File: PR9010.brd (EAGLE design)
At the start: 100 x 80 mm, 58 parts, among them J1 AVR_SPI_PRG_6NS, U1 SI4703, U2 Tiny85-20-SMT, Y1 32.768kHz

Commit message: Sch Updates
Continuing to update the PR9010 sch
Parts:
- removed ESD: CM1213A-01S, PubRadioLib:SOT23-3
- added D1: (no value), SparkFun-DiscreteSemi:SOT23
- added U$1, U$2: BK-92_MPD_AA_BATT_CLIP, PR_Libraries:BK-92_MPD_AA_BATT_CLIP
- moved LID 139.4 mm to (64.3, 32.0)
- moved GND 128.5 mm to (53.6, 6.86)
- moved AMP_O 125.3 mm to (36.8, 9.40), turned to 270 degrees
- moved GND33 118.9 mm to (53.6, 10.4)
- moved C18 115.6 mm to (29.0, 4.06), turned to 270 degrees
- moved U$5 113.6 mm to (47.5, 50.3), turned to 270 degrees
- moved C17 108.2 mm to (22.1, 10.9)
- moved GND31 108.1 mm to (53.6, 14.2)
- moved C16 106.3 mm to (22.1, 8.89)
- moved C9 106.1 mm to (32.5, 9.40)
- moved R1 105.6 mm to (65.0, 29.0), turned to 180 degrees
- moved C11 104.7 mm to (26.2, 11.9), turned to 90 degrees
- moved C10 100.7 mm to (24.6, 50.5), turned to 270 degrees
- moved C20 100.5 mm to (65.0, 26.2), turned to 180 degrees
- moved C12 100.3 mm to (22.1, 4.83)
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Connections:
- removed net N$10: C1.1, C13.1, C2.1, C6.1, L3.2
- removed net N$19: ANT.P$1, C10.1, C8.1, ESD.1
- new net N$13: U$1.NEG, U$1.NEG@2, U$2.POS, U$2.POS@2
- new net N$14: ANT.P$1, D1.1
- new net N$15: PWRIN.1, U$1.POS, U$1.POS@2, U$5.SW_OUT
- new net N$17: C10.1, C8.1, D1.2
- net 3.3V: no longer PWRIN.1, U$5.SW_OUT
- net GND: now also D1.3, U$2.NEG, U$2.NEG@2; no longer ESD.2, ESD.3
- net N$9: now also C1.1, C13.1, C2.1, C6.1, L3.2
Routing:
- net SDIO: track 0.00 -> 49.5 mm, vias 0 -> 2
- net SCLK: track 0.00 -> 49.0 mm
- net 3.3V: track 0.00 -> 24.4 mm, vias 0 -> 4
- net N$9: track 0.00 -> 15.6 mm, vias 0 -> 2
- net !RST-L: track 0.00 -> 14.3 mm
- net N$18: track 0.00 -> 14.0 mm
- net SDIO-L: track 0.00 -> 12.7 mm
- net PB1: track 0.00 -> 12.6 mm, vias 0 -> 2
- net !SEN-L: track 0.00 -> 12.2 mm
- net VCC: track 0.00 -> 12.0 mm
- net SCLK-L: track 0.00 -> 11.6 mm
- net !RST: track 0.00 -> 9.50 mm
- net !SEN: track 0.00 -> 9.18 mm
- net PB5: track 0.00 -> 8.56 mm
- net N$1: track 0.00 -> 8.31 mm
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- added copper zone on layer 1, net GND
- added copper zone on layer 16, net GND
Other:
- board size 100 x 80 mm -> 71.6 x 80 mm

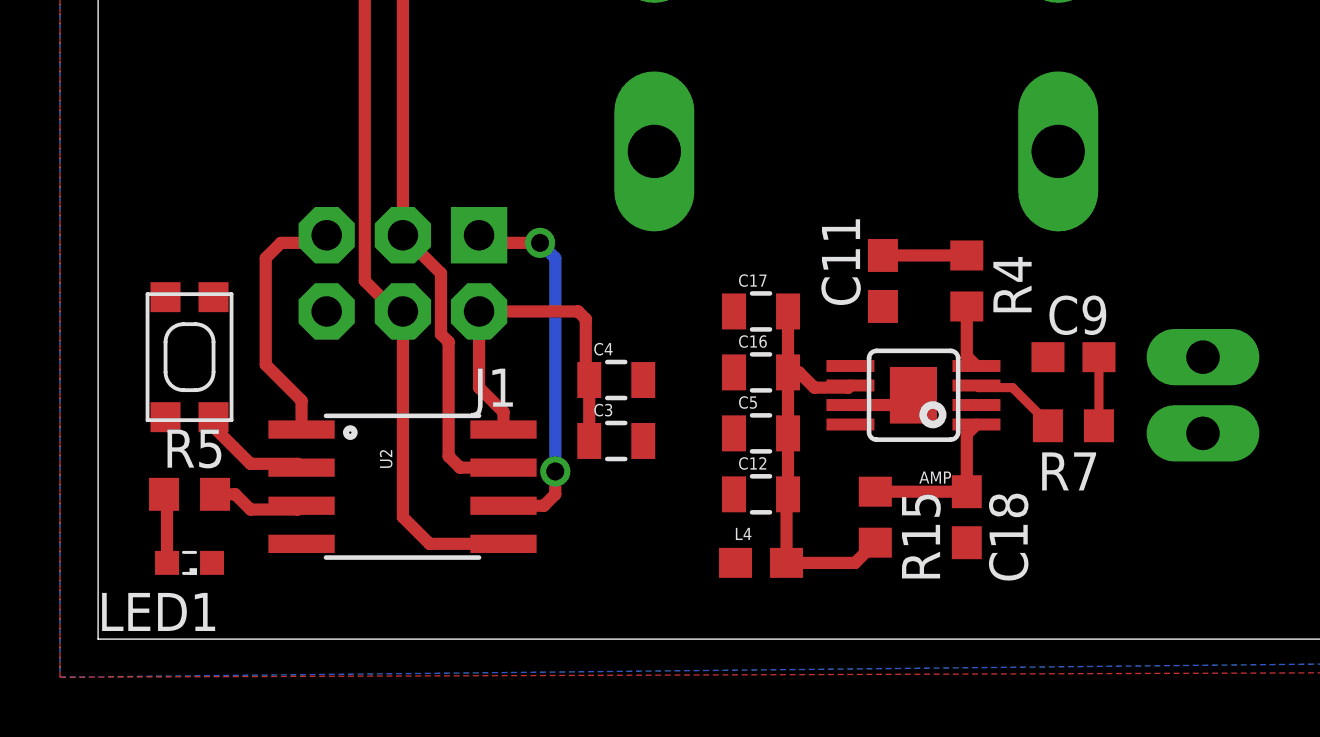
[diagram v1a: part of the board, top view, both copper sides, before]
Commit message: fixed prefixes
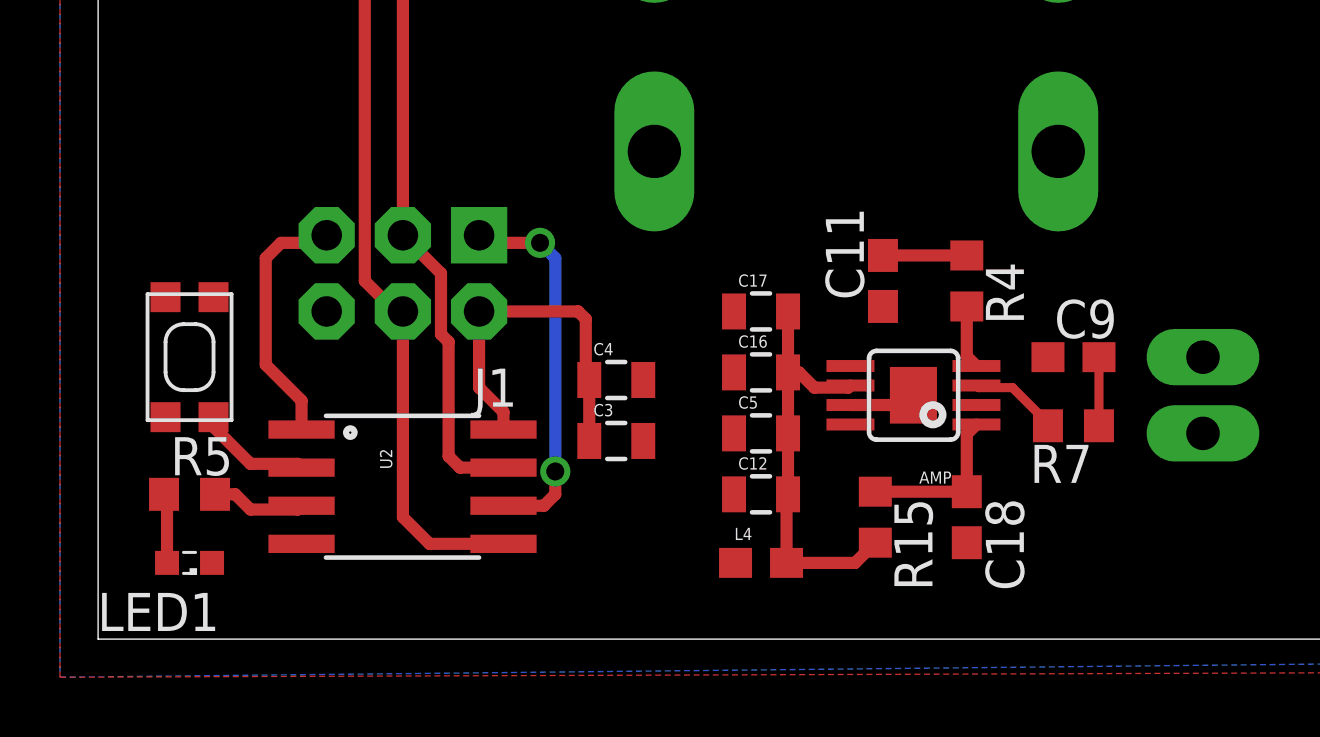
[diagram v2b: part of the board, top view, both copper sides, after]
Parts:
- C1, C10, C13, C2, C6, C8: value (none) -> 1.0uF
- C14: value 4.7uF -> 1.0uF
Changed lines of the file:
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@@
 <?xml version="1.0" encoding="utf-8"?>
 <!DOCTYPE eagle SYSTEM "eagle.dtd">
-<eagle version="6.6.0">
+<eagle version="7.2.0">
 <drawing>
 <settings>
@@
 <pass name="Default">
 <param name="RoutingGrid" value="50mil"/>
+<param name="AutoGrid" value="1"/>
+<param name="Efforts" value="0"/>
+<param name="TopRouterVariant" value="1"/>
 <param name="tpViaShape" value="round"/>
 <param name="PrefDir.1" value="|"/>
@@
 <element name="LED1" library="led" package="SML0603" value="" x="3.048" y="2.54" rot="R180"/>
 <element name="R5" library="resistor" package="R0603" value="1K" x="3.048" y="4.826"/>
-<element name="C8" library="SparkFun-Capacitors" package="0805" value="" x="21.59" y="51.816" rot="R180">
+<element name="C8" library="SparkFun-Capacitors" package="0805" value="1.0uF" x="21.59" y="51.816" rot="R180">
 <attribute name="PROD_ID" value="CAP-11625" x="-46.99" y="129.286" size="1.778" layer="27" rot="R180" display="off"/>
 </element>
 <element name="L1" library="SparkFun-Passives" package="0805" value="" x="21.59" y="49.53" rot="R180"/>
-<element name="C10" library="SparkFun-Capacitors" package="0805" value="" x="24.638" y="50.546" rot="R270">
+<element name="C10" library="SparkFun-Capacitors" package="0805" value="1.0uF" x="24.638" y="50.546" rot="R270">
 <attribute name="PROD_ID" value="CAP-11625" x="-52.832" y="-21.844" size="1.778" layer="27" rot="R270" display="off"/>
 </element>
-<element name="C13" library="SparkFun-Capacitors" package="0805" value="" x="27.94" y="39.116">
+<element name="C13" library="SparkFun-Capacitors" package="0805" value="1.0uF" x="27.94" y="39.116">
 <attribute name="PROD_ID" value="CAP-11625" x="43.18" y="-42.164" size="1.778" layer="27" display="off"/>
 </element>
-<element name="C1" library="SparkFun-Capacitors" package="0805" value="" x="27.94" y="45.974">
+<element name="C1" library="SparkFun-Capacitors" package="0805" value="1.0uF" x="27.94" y="45.974">
 <attribute name="PROD_ID" value="CAP-11625" x="85.09" y="-31.496" size="1.778" layer="27" display="off"/>
 </element>
-<element name="C2" library="SparkFun-Capacitors" package="0805" value="" x="27.94" y="44.45">
+<element name="C2" library="SparkFun-Capacitors" package="0805" value="1.0uF" x="27.94" y="44.45">
 <attribute name="PROD_ID" value="CAP-11625" x="88.9" y="-33.02" size="1.778" layer="27" display="off"/>
 </element>
-<element name="C6" library="SparkFun-Capacitors" package="0805" value="" x="27.94" y="40.894">
+<element name="C6" library="SparkFun-Capacitors" package="0805" value="1.0uF" x="27.94" y="40.894">
 <attribute name="PROD_ID" value="CAP-11625" x="92.71" y="-36.576" size="1.778" layer="27" display="off"/>
 </element>
 <element name="PWRIN" library="SparkFun-Connectors" package="1X02_LONGPADS" value="M02PTH3" x="30.988" y="75.438"/>
-<element name="C14" library="SparkFun-Capacitors" package="0805" value="4.7uF" x="18.034" y="42.418" rot="R270">
+<element name="C14" library="SparkFun-Capacitors" package="0805" value="1.0uF" x="18.034" y="42.418" rot="R270">
 <attribute name="PROD_ID" value="CAP-11625" x="-55.626" y="-12.192" size="1.778" layer="27" rot="R270" display="off"/>
 </element>

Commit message: Prefix changes
Prefix changes
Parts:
- removed AMP: TPA2005D1DGN, SparkFun-AnalogIC:POWER-SOP8
- removed ANT: M3_SCREW_POST, PR_Libraries:M3_SCREW_POST
- removed L4: 2.5 kOhm @ 100MHz, SparkFun-Passives:0603
- removed U$5: RV170SF_TAIWANA_POT_SW, PR_Libraries:RV170SF_TAIWANA_POT_SW
- added J2: AVR_SPI_PRG_6NS, SparkFun-Connectors:2X3-NS
- added L2: 2.5k@100MHz, SparkFun-Passives:0603
- added R11: 40.2K, resistor:R0603
- added U3: Tiny85-20-SMT, SparkFun-DigitalIC:SO08-EIAJ
- C1: value 1.0uF -> 220uF; device SparkFun-Capacitors:0805 -> SparkFun-Passives:PANASONIC_C
- C11, C9: value .033uf -> 1.0uF; device resistor:C0603 -> SparkFun-Capacitors:0805
- C12: value 10uf -> .1uf
- C13: value 1.0uF -> .033uf; device SparkFun-Capacitors:0805 -> resistor:C0603
- C14: value 1.0uF -> 10uf; device SparkFun-Capacitors:0805 -> SparkFun-Passives:0805
- C15: value 22pf -> 10uf; device SparkFun-Passives:0805 -> resistor:C0603
- C16: value 100nF -> .033uf; device SparkFun-Passives:0805 -> resistor:C0603
- C17: value 100pf -> 1uf
- C18: device resistor:C0603 -> SparkFun-Passives:0805
- C19: value 220uF -> .1uf; device SparkFun-Passives:PANASONIC_C -> SparkFun-Passives:0805
- C20: value (none) -> 100pf
- C3: value .1uf -> 1.0uF; device SparkFun-Passives:0805 -> SparkFun-Capacitors:0805
- C4: value 10uf -> 22pf
- C5: value 1uf -> 22pf
- C6: value 1.0uF -> (none); device SparkFun-Capacitors:0805 -> SparkFun-Passives:0805
- C7: value 22pf -> 1.0uF; device SparkFun-Passives:0805 -> SparkFun-Capacitors:0805
- J1: value AVR_SPI_PRG_6NS -> M3_SCREW_POST; device SparkFun-Connectors:2X3-NS -> PR_Libraries:M3_SCREW_POST
- L3: value 2.5k@100MHz -> 2.5 kOhm @ 100MHz
- R1: value (none) -> RV170SF_TAIWANA_POT_SW; device SparkFun-Passives:0805 -> PR_Libraries:RV170SF_TAIWANA_POT_SW
- R10: value 10K -> (none)
- R13: value 4.7K -> 40.2K; device SparkFun-Passives:0805 -> resistor:R0603
- R14: value 4.7K -> 1K; device SparkFun-Passives:0805 -> resistor:R0603
- R4: value 40.2K -> 330; device resistor:R0603 -> SparkFun-Passives:0805
- R5: value 1K -> 330; device resistor:R0603 -> SparkFun-Passives:0805
- R6: value 4.7K -> 10K
- R7: value 40.2K -> 4.7K; device resistor:R0603 -> SparkFun-Passives:0805
- R8, R9: value 330 -> 4.7K
- U2: value Tiny85-20-SMT -> TPA2005D1DGN; device SparkFun-DigitalIC:SO08-EIAJ -> SparkFun-AnalogIC:POWER-SOP8
- moved J1 58.9 mm to (9.14, 71.1), turned to 0 degrees
- moved R10 57.2 mm to (65.0, 29.0), turned to 180 degrees
- moved C20 45.6 mm to (22.1, 10.9), turned to 0 degrees
- moved C3 44.6 mm to (24.6, 50.5), turned to 270 degrees
- moved R14 44.4 mm to (3.05, 4.83), turned to 0 degrees
- moved L3 40.6 mm to (22.1, 2.54), turned to 0 degrees
- moved R7 40.4 mm to (12.4, 42.2), turned to 270 degrees
- moved C6 39.9 mm to (65.0, 26.2), turned to 180 degrees
- moved C15 39.2 mm to (29.0, 4.06), turned to 270 degrees
- moved R4 38.1 mm to (10.4, 45.2)
- moved R5 38.1 mm to (10.4, 42.2), turned to 270 degrees
- moved C9 36.1 mm to (18.0, 42.4), turned to 270 degrees
- moved C5 35.6 mm to (24.4, 42.4), turned to 180 degrees
- moved R13 34.4 mm to (29.0, 11.9)
- moved C4 34.0 mm to (21.1, 42.4)
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- renumbered AMP_O to JP13, FET to FET1, FMIC_IO to JP1, FM_AOUT to JP12, GND to JP9, GND29 to JP11, GND31 to JP8, GND33 to JP10, LID to JP7, PWRIN to JP4, R15 to R12, SCLK_BUS to JP3, SDIO_BUS to JP2, STA_CH to SW1, U$1 to JP5, U$2 to JP6
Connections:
- net !RST: now also R2.2; no longer R9.2
- net !RST-L: now also R2.1, R6.2; no longer R10.2, R9.1
- net !SEN: now also R3.2; no longer R8.2
- net !SEN-L: now also R3.1, R9.1; no longer R14.1, R8.1
- net 3.3V: now also R7.2, R8.2, R9.2; no longer R13.2, R14.2, R6.2
- net A_IN: now also C9.2, R1.SIGNAL; no longer C14.2, U$5.SIGNAL
- net A_OUT: now also C13.1, R1.WIPER; no longer C9.1, U$5.WIPER
- net GND: now also C1.-, C10.2, C11.2, C12.2, C14.2, C18.1, C19.1, C20.1, C5.2, J2.6, R1.GND, R6.1, U2.7, U2.9, U3.4; no longer AMP.7, AMP.9, C1.2, C11.1, C12.1, C13.2, C18.2, C19.-, C20.2, C3.2, C5.1, J1.6, R10.1, U$5.GND, U2.4
- net LOUT: now also C9.1; no longer C14.1
- net N$1: now also C4.1; no longer C15.1
- net N$11: now also U3.2; no longer U2.2
- net N$12: now also R14.2, U3.3; no longer R5.2, U2.3
- net N$14: now also J1.P$1; no longer ANT.P$1
- net N$15: now also R1.SW_OUT; no longer U$5.SW_OUT
- net N$17: now also C2.1, C3.1; no longer C10.1, C8.1
- net N$18: now also C18.2, C19.2, C20.2, L3.2, U2.6; no longer AMP.6, C12.2, C16.2, C5.2, L4.2
- net N$2: now also C5.1; no longer C7.1
- net N$20: now also C15.1, U2.1; no longer AMP.1, C18.1
- net N$23: now also C16.2, R13.1; no longer C11.2, R4.1
- net N$3: now also C13.2, R11.1; no longer C9.2, R7.1
- net N$34: now also R1.SW_IN; no longer U$5.SW_IN
- net N$35: now also C6.1, R10.1; no longer C20.1, R1.1
- net N$4: now also R11.2, U2.3; no longer AMP.3, R7.2
- net N$5: now also R13.2, U2.4; no longer AMP.4, R4.2
- net N$6: now also C3.2; no longer C10.2
- net N$7: now also R14.1; no longer R5.1
- net N$8: now also R10.2; no longer R1.2
- net N$9: now also C10.1, C11.1, C7.1, C8.1, L2.2; no longer C1.1, C13.1, C2.1, C6.1, L3.2
- net OUT+: now also U2.5; no longer AMP.5
- net OUT-: now also U2.8; no longer AMP.8
- net PB1: now also J2.1, U3.6; no longer J1.1, U2.6
- net PB5: now also J2.5, U3.1; no longer J1.5, U2.1
- net SCLK: now also J2.3, R4.2, U3.7; no longer J1.3, R3.2, U2.7
- net SCLK-L: now also R4.1, R8.1; no longer R3.1, R6.1
- net SDIO: now also J2.4, R5.2, U3.5; no longer J1.4, R2.2, U2.5
- net SDIO-L: now also R5.1, R7.1; no longer R13.1, R2.1
- net VCC: now also C1.+, C12.1, C14.1, J2.2, L2.1, U3.8; no longer C19.+, C3.1, C4.1, J1.2, L4.1, U2.8

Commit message: Updated Sch & Layout
Began layout on the test board
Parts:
- added U$3: CE32A_DAYTON_SPKR, PR_Libraries:CE32A_DAYTON_SPKR
- moved LED1 92.0 mm to (70.4, 65.3), turned to 270 degrees
- moved J2 92.0 mm to (86.9, 63.0), turned to 270 degrees
- moved SW1 90.0 mm to (77.0, 60.7), turned to 135 degrees
- moved R14 88.3 mm to (70.4, 62.0), turned to 270 degrees
- moved JP6 82.3 mm to (100.8, 40.1), turned to 90 degrees
- moved U3 80.5 mm to (66.3, 62.7), turned to 0 degrees
- moved C14 70.6 mm to (61.7, 63.5), turned to 180 degrees
- moved C12 70.4 mm to (61.7, 61.2), turned to 180 degrees
- moved JP5 58.6 mm to (76.7, 78.5), turned to 0 degrees
- moved JP13 52.8 mm to (89.4, 13.7)
- moved JP8 50.1 mm to (3.81, 8.38)
- moved JP10 50.1 mm to (3.81, 15.7)
- moved JP9 50.1 mm to (3.81, 12.2)
- moved JP11 49.8 mm to (3.81, 19.6)
- moved J1 37.9 mm to (27.7, 38.1)
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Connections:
- net OUT+: now also U$3.-
- net OUT-: now also U$3.+
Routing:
- net N$15: track 0.00 -> 56.2 mm
- net SDIO: track 49.5 -> 0.00 mm, vias 2 -> 0
- net SCLK: track 49.0 -> 0.18 mm
- net N$13: track 0.00 -> 31.3 mm
- net 3.3V: track 24.4 -> 4.83 mm, vias 4 -> 3
- net PB1: track 12.6 -> 0.00 mm, vias 2 -> 0
- net !RST-L: track 14.3 -> 2.03 mm
- net SDIO-L: track 12.7 -> 2.03 mm
- net !SEN-L: track 12.2 -> 2.03 mm
- net SCLK-L: track 11.6 -> 2.03 mm
- net !RST: track 9.50 -> 0.00 mm
- net !SEN: track 9.18 -> 0.00 mm
- net PB5: track 8.56 -> 0.00 mm
- net N$4: track 2.99 -> 9.69 mm
- net VCC: track 12.0 -> 5.61 mm
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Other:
- board size 71.6 x 80 mm -> 108.7 x 86.4 mm
